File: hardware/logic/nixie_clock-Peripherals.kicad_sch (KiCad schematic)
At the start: 19 parts, among them SW1 SW_Push, SW5 RotaryEncoder_Switch, U2 DS3234

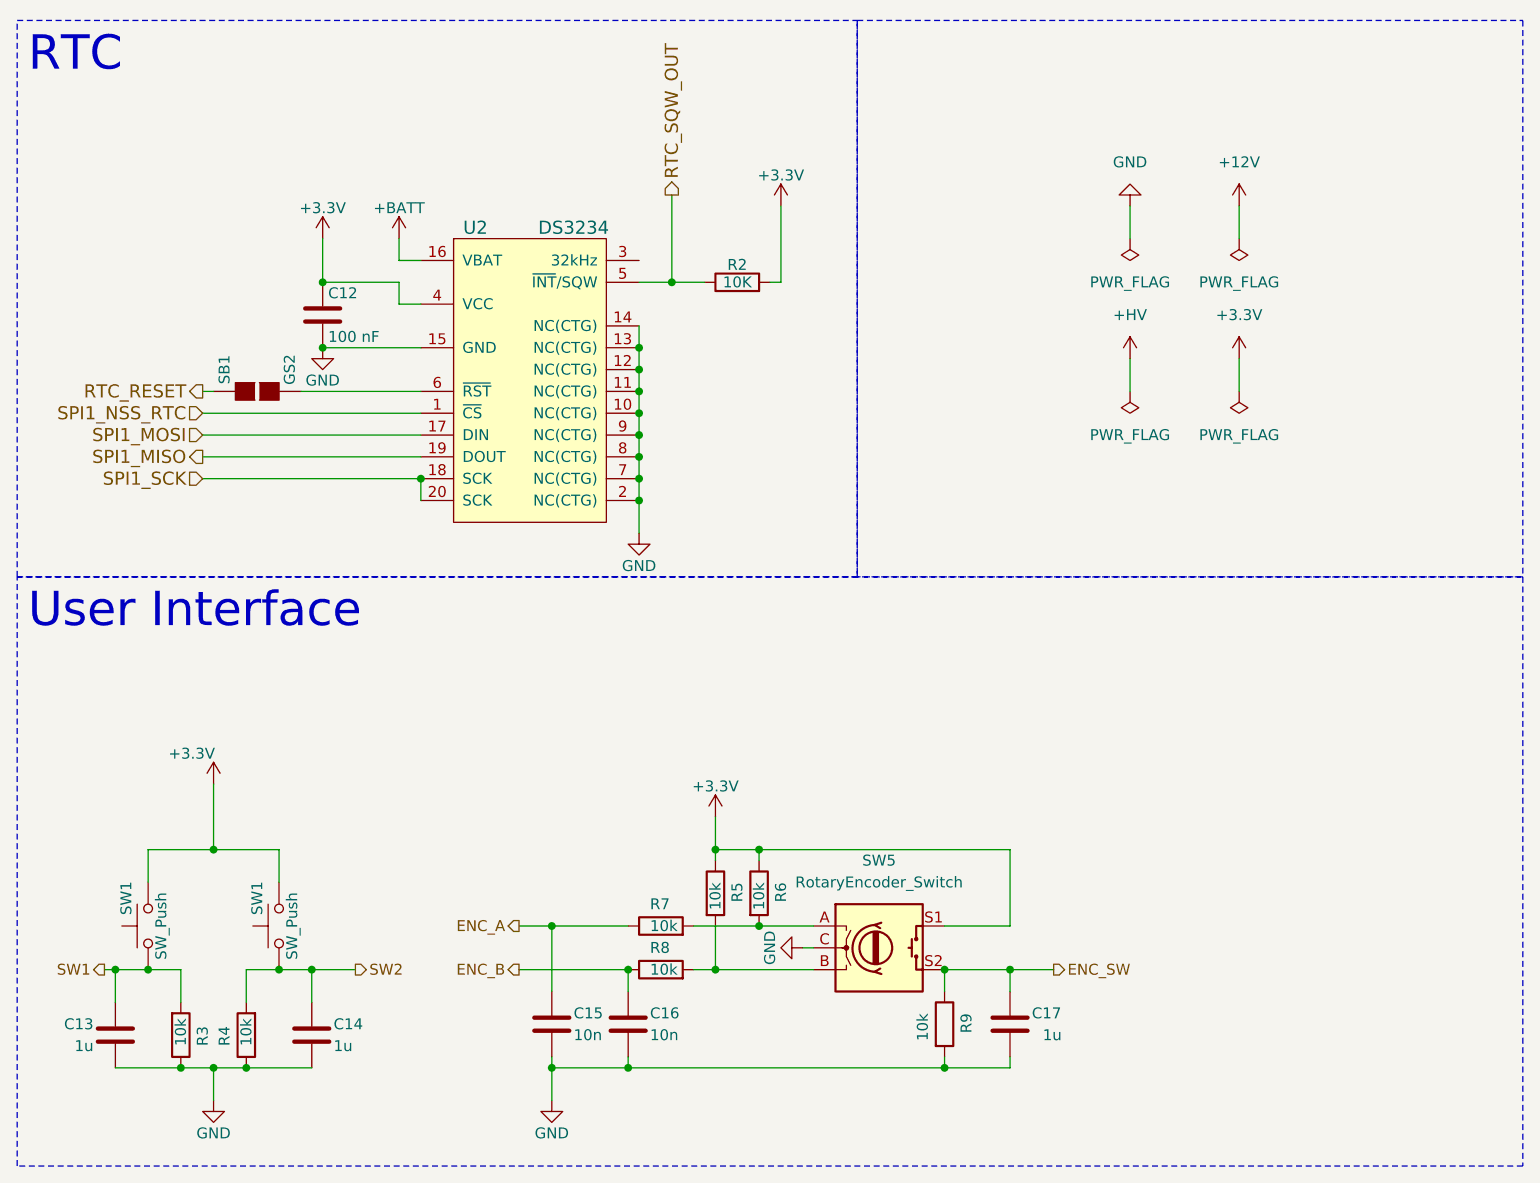
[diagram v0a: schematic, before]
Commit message: Inital PCB placement
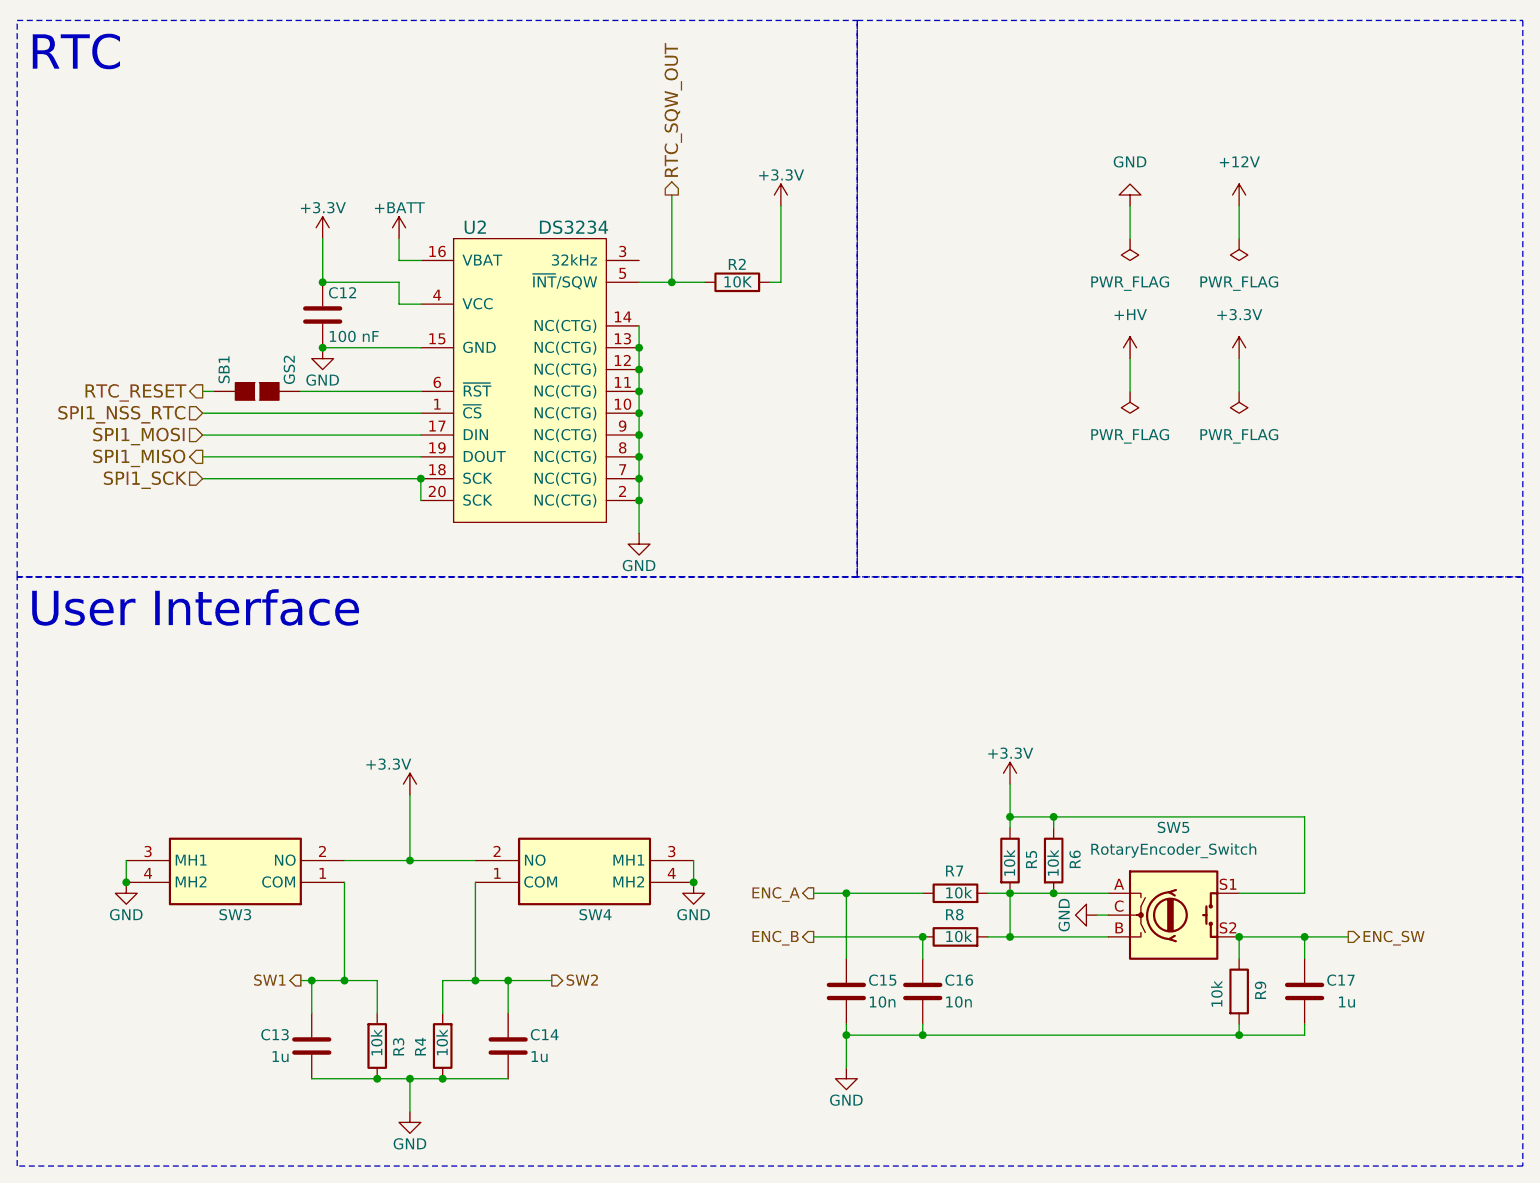
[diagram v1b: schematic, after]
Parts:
- removed SW1 (x2): SW_Push, Button_Switch_SMD:SW_Push_1P1T_NO_CK_KSC6xxJ, symbol Switch:SW_Push
- added SW3, SW4: FSMRA4JH04, FSMRA4JH04, symbol FSMRA4JH04:FSMRA4JH04
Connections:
- net +3V3: now also SW3.2 (NO), SW4.2 (NO)
- net GND: now also SW3.3 (MH1), SW3.4 (MH2), SW4.3 (MH1), SW4.4 (MH2)
- net SW1: now also SW3.1 (COM)
- net SW2: now also SW4.1 (COM)
- net at R6.2, R7.2, SW5.A: now also R5.2, R8.2, SW5.B
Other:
- moved on the sheet: C13, C14, C15, C16, C17, R3, R4, R5, R6, R7, R8, R9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

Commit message: Troubleshooting logic board design, begin component placement, fix positioning of board connectors
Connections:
- net at R6.2, R7.2, SW5.A: no longer R5.2, R8.2, SW5.B
- new net: R5.2, R8.2, SW5.B
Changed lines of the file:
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@@
   (junction (at 86.36 57.15) (diameter 0) (color 0 0 0 0)
   )
-  (junction (at 129.54 115.57) (diameter 0) (color 0 0 0 0)
-  )
   (junction (at 86.36 64.77) (diameter 0) (color 0 0 0 0)
   )
@@
     (stroke (width 0) (type default))
   )
-  (wire (pts (xy 129.54 115.57) (xy 134.62 115.57))
+  (wire (pts (xy 127 115.57) (xy 134.62 115.57))
     (stroke (width 0) (type default))
   )
@@
   )
   (wire (pts (xy 60.96 69.85) (xy 60.96 67.31))
-    (stroke (width 0) (type default))
-  )
-  (wire (pts (xy 127 115.57) (xy 129.54 115.57))
     (stroke (width 0) (type default))
   )
@@
     (effects (font (size 4 4)) (justify left bottom))
   )
+  (label "S1" (at 160.02 115.57 0) (fields_autoplaced)
+    (effects (font (size 1.27 1.27)) (justify left bottom))
+  )
   (hierarchical_label "SPI1_SCK" (shape input) (at 35.56 67.31 180) (fields_autoplaced)
